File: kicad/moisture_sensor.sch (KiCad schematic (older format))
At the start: 17 parts, among them IC3 TLC555CDR, IC4 ADC081C021CIMK_NOPB, J11 SOIL_I2C, J18 ALWAYS_ON, Q1 DTC113Z

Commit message: Libraries cleanup
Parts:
- IC3: footprint SamacSys:SOIC127P600X175-8N -> SamacSys_Parts:SOIC127P600X175-8N; symbol SamaSys:TLC555CDR -> SamacSys_Parts:TLC555CDR
- IC4: footprint SamacSys:SOT95P280X110-6N -> SamacSys_Parts:SOT95P280X110-6N; symbol SamaSys:ADC081C021CIMK_NOPB -> SamacSys_Parts:ADC081C021CIMK_NOPB
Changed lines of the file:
@@
 $Descr A4 11693 8268
 encoding utf-8
-Sheet 3 6
+Sheet 3 7
 Title ""
 Date ""
@@
 	7450 3950 7450 4350
 $Comp
-L SamaSys:TLC555CDR IC3
+L SamacSys_Parts:TLC555CDR IC3
 U 1 1 5F161298
 P 7550 3850
 F 0 "IC3" H 8150 3850 50  0000 C CNN
 F 1 "TLC555CDR" H 8150 3400 50  0000 C CNN
-F 2 "SamacSys:SOIC127P600X175-8N" H 8600 3950 50  0001 L CNN
+F 2 "SamacSys_Parts:SOIC127P600X175-8N" H 8600 3950 50  0001 L CNN
 F 3 "" H 8600 3850 50  0001 L CNN
 F 4 "TLC555CDR, Timer 2MHz, 2 ??? 15 V, 8-Pin SOIC-8" H 8600 3750 50  0001 L CNN "Description"
@@
 	7150 2750 7600 2750
 $Comp
-L SamaSys:ADC081C021CIMK_NOPB IC4
+L SamacSys_Parts:ADC081C021CIMK_NOPB IC4
 U 1 1 5EFC5A0F
 P 7600 2550
 F 0 "IC4" H 8150 2815 50  0000 C CNN
 F 1 "ADC081C021CIMK_NOPB" H 8150 2724 50  0000 C CNN
-F 2 "SamacSys:SOT95P280X110-6N" H 8550 2650 50  0001 L CNN
+F 2 "SamacSys_Parts:SOT95P280X110-6N" H 8550 2650 50  0001 L CNN
 F 3 "http://www.ti.com/lit/ds/symlink/adc081c021.pdf" H 8550 2550 50  0001 L CNN
 F 4 "I2C-Compatible, 8-Bit Analog-to-Digital Converter with Alert Pin" H 8550 2450 50  0001 L CNN "Description"

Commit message: Comitting yesterday's leftovers
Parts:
- renumbered C3 to C5, C7 to C6, C4 to C7, C5 to C8, D1 to D4, IC3 to IC1, IC4 to IC2, J11 to J7, J18 to J8, R5 to R14, R4 to R15
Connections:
- net VA renamed +3.3VA
- net VDD renamed +3V3
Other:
- moved on the sheet: C5, C6, C7, C8, Cref1, D4, FB1, FB2, IC1, IC2, J7, J8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

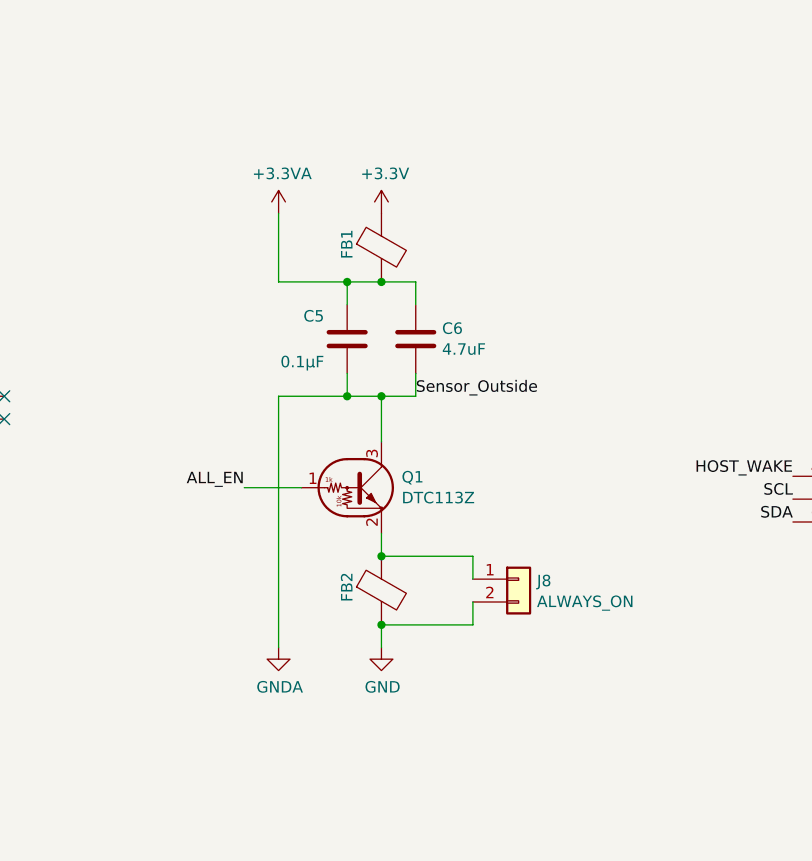
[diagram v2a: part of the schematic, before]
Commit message: Mapped footprints, PCB in progress
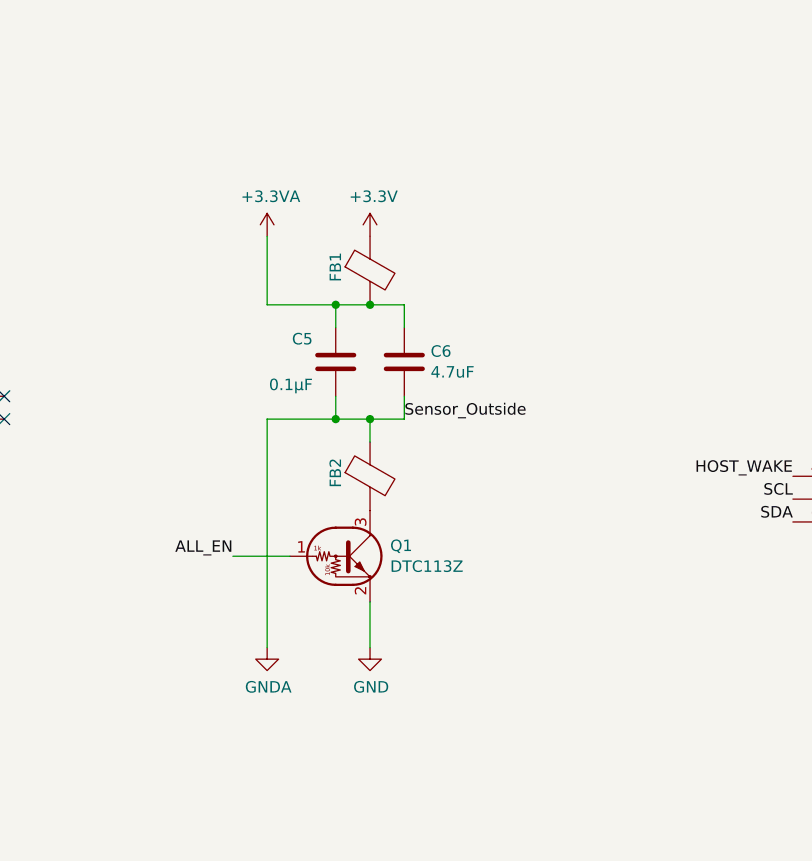
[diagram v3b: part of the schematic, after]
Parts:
- removed J8: ALWAYS_ON, Connector_PinHeader_2.54mm:PinHeader_1x02_P2.54mm_Vertical, symbol Connector_Generic:Conn_01x02
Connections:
- net GND: now also Q1.2 (E); no longer FB2.2
- net GNDA: now also FB2.1; no longer Q1.3 (C)
- new net: FB2.2, Q1.3 (C)
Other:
- moved on the sheet: C5, C6, FB1, FB2, Q1
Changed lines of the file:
@@
 L Device:C C5
 U 1 1 5F16FB60
-P 4050 3450
-F 0 "C5" H 4150 3350 50  0000 L CNN
-F 1 "0.1μF" H 4150 3550 50  0000 L CNN
-F 2 "Capacitor_SMD:C_1206_3216Metric" H 4088 3300 50  0001 C CNN
-F 3 "~" H 4050 3450 50  0001 C CNN
-	1    4050 3450
+P 4000 3550
+F 0 "C5" H 4100 3450 50  0000 L CNN
+F 1 "0.1μF" H 4100 3650 50  0000 L CNN
+F 2 "Capacitor_SMD:C_1206_3216Metric" H 4038 3400 50  0001 C CNN
+F 3 "~" H 4000 3550 50  0001 C CNN
+	1    4000 3550
 	-1   0    0    1
 $EndComp
@@
 	8750 3600 9500 3600
 Wire Wire Line
-	4350 3600 4350 3700
-Wire Wire Line
-	4050 3700 4050 3600
-Wire Wire Line
-	4050 3200 4050 3300
+	4300 3700 4300 3800
+Wire Wire Line
+	4000 3800 4000 3700
+Wire Wire Line
+	4000 3300 4000 3400
 Text Label 8550 4050 3    50   ~ 0
 Sensor_Inside
-Text Label 4350 3700 0    50   ~ 0
+Text Label 4300 3800 0    50   ~ 0
 Sensor_Outside
 Text Notes 7400 7500 0    50   ~ 0
@@
 Moisture Sensor
 $Comp
-L Transistor_BJT:DTC113Z Q1
-U 1 1 5F30B926
-P 4100 4100
-F 0 "Q1" H 4288 4146 50  0000 L CNN
-F 1 "DTC113Z" H 4288 4055 50  0000 L CNN
-F 2 "Parts:DTC113ZEBTL" H 4100 4100 50  0001 L CNN
-F 3 "" H 4100 4100 50  0001 L CNN
-	1    4100 4100
-	1    0    0    -1
-$EndComp
-$Comp
 L Device:Ferrite_Bead FB1
 U 1 1 5F30F8CD
-P 4200 3050
-F 0 "FB1" V 4050 3000 50  0000 L CNN
-F 1 "BLM21AG601SZ1D" V 4350 2900 50  0001 L CNN
-F 2 "Parts:Ferrite_Bead_0805_BLM21" V 4130 3050 50  0001 C CNN
-F 3 "https://www.mouser.com/datasheet/2/281/QNFA9114-1485065.pdf" H 4200 3050 50  0001 C CNN
-	1    4200 3050
-	1    0    0    -1
-$EndComp
-Wire Wire Line
-	4350 3200 4200 3200
-Connection ~ 4200 3200
-Wire Wire Line
-	4200 3200 4050 3200
+P 4150 3150
+F 0 "FB1" V 4000 3100 50  0000 L CNN
+F 1 "BLM21AG601SZ1D" V 4300 3000 50  0001 L CNN
+F 2 "Parts:Ferrite_Bead_0805_BLM21" V 4080 3150 50  0001 C CNN
+F 3 "https://www.mouser.com/datasheet/2/281/QNFA9114-1485065.pdf" H 4150 3150 50  0001 C CNN
+	1    4150 3150
+	1    0    0    -1
+$EndComp
+Wire Wire Line
+	4300 3300 4150 3300
+Connection ~ 4150 3300
+Wire Wire Line
+	4150 3300 4000 3300
 $Comp
 L power:GND #PWR?
@@
 NoConn ~ 2550 3700
 NoConn ~ 2550 3800
-Text Label 3600 4100 2    50   ~ 0
+Text Label 3550 4400 2    50   ~ 0
 ALL_EN
 $Comp
@@
 $EndComp
 Wire Wire Line
-	4350 3300 4350 3200
+	4300 3400 4300 3300
 $Comp
 L Device:C C6
 U 1 1 5FCEA2F8
-P 4350 3450
-F 0 "C6" H 4465 3496 50  0000 L CNN
-F 1 "4.7uF" H 4465 3405 50  0000 L CNN
-F 2 "Capacitor_SMD:C_1206_3216Metric" H 4388 3300 50  0001 C CNN
-F 3 "~" H 4350 3450 50  0001 C CNN
-	1    4350 3450
-	1    0    0    -1
-$EndComp
-Wire Wire Line
-	3600 4100 3850 4100
+P 4300 3550
+F 0 "C6" H 4415 3596 50  0000 L CNN
+F 1 "4.7uF" H 4415 3505 50  0000 L CNN
+F 2 "Capacitor_SMD:C_1206_3216Metric" H 4338 3400 50  0001 C CNN
+F 3 "~" H 4300 3550 50  0001 C CNN
+	1    4300 3550
+	1    0    0    -1
+$EndComp
 $Comp
 L power:+3.3V #PWR035
@@
 L power:+3.3V #PWR031
 U 1 1 6115F35B
-P 4200 2900
-F 0 "#PWR031" H 4200 2750 50  0001 C CNN
-F 1 "+3.3V" H 4215 3073 50  0000 C CNN
-F 2 "" H 4200 2900 50  0001 C CNN
-F 3 "" H 4200 2900 50  0001 C CNN
-	1    4200 2900
-	1    0    0    -1
-$EndComp
-Wire Wire Line
-	4050 3700 4200 3700
-Wire Wire Line
-	4200 3700 4200 3900
-Connection ~ 4200 3700
-Wire Wire Line
-	4200 3700 4350 3700
+P 4150 3000
+F 0 "#PWR031" H 4150 2850 50  0001 C CNN
+F 1 "+3.3V" H 4165 3173 50  0000 C CNN
+F 2 "" H 4150 3000 50  0001 C CNN
+F 3 "" H 4150 3000 50  0001 C CNN
+	1    4150 3000
+	1    0    0    -1
+$EndComp
 $Comp
 L power:GNDA #PWR028
@@
 $EndComp
 Wire Wire Line
-	4050 3700 3750 3700
-Connection ~ 4050 3700
+	4000 3800 3700 3800
+Connection ~ 4000 3800
 Text Label 6000 4050 2    50   ~ 0
 HOST_WAKE
@@
 L power:+3.3VA #PWR030
 U 1 1 611E3CB4
-P 3750 2900
-F 0 "#PWR030" H 3750 2750 50  0001 C CNN
-F 1 "+3.3VA" H 3765 3073 50  0000 C CNN
-F 2 "" H 3750 2900 50  0001 C CNN
-F 3 "" H 3750 2900 50  0001 C CNN
-	1    3750 2900
-	1    0    0    -1
-$EndComp
-Wire Wire Line
-	3750 2900 3750 3200
-Connection ~ 4050 3200
+P 3700 3000
+F 0 "#PWR030" H 3700 2850 50  0001 C CNN
+F 1 "+3.3VA" H 3715 3173 50  0000 C CNN
+F 2 "" H 3700 3000 50  0001 C CNN
+F 3 "" H 3700 3000 50  0001 C CNN
+	1    3700 3000
+	1    0    0    -1
+$EndComp
+Wire Wire Line
+	3700 3000 3700 3300
+Connection ~ 4000 3300
 $Comp
 L power:+3.3VA #PWR033
@@
 L power:GNDA #PWR036
 U 1 1 61222E66
-P 3750 4800
-F 0 "#PWR036" H 3750 4550 50  0001 C CNN
-F 1 "GNDA" H 3755 4627 50  0000 C CNN
-F 2 "" H 3750 4800 50  0001 C CNN
-F 3 "" H 3750 4800 50  0001 C CNN
-	1    3750 4800
-	1    0    0    -1
-$EndComp
-Wire Wire Line
-	3750 3700 3750 4800
-Wire Wire Line
-	3750 3200 4050 3200
-Wire Wire Line
-	4200 4300 4200 4400
-Wire Wire Line
-	4600 4700 4200 4700
-Wire Wire Line
-	4600 4600 4600 4700
-Wire Wire Line
-	4600 4400 4600 4500
-Wire Wire Line
-	4200 4400 4600 4400
-$Comp
-L Connector_Generic:Conn_01x02 J8
-U 1 1 5F4FBEBB
-P 4800 4500
-F 0 "J8" H 4880 4492 50  0000 L CNN
-F 1 "ALWAYS_ON" H 4880 4401 50  0000 L CNN
-F 2 "Connector_PinHeader_2.54mm:PinHeader_1x02_P2.54mm_Vertical" H 4800 4500 50  0001 C CNN
-F 3 "~" H 4800 4500 50  0001 C CNN
-	1    4800 4500
+P 3700 4800
+F 0 "#PWR036" H 3700 4550 50  0001 C CNN
+F 1 "GNDA" H 3705 4627 50  0000 C CNN
+F 2 "" H 3700 4800 50  0001 C CNN
+F 3 "" H 3700 4800 50  0001 C CNN
+	1    3700 4800
+	1    0    0    -1
+$EndComp
+Wire Wire Line
+	3700 3300 4000 3300
+Wire Wire Line
+	4000 3800 4150 3800
+Wire Wire Line
+	4150 4600 4150 4800
+$Comp
+L power:GND #PWR037
+U 1 1 5F30EBF5
+P 4150 4800
+F 0 "#PWR037" H 4150 4550 50  0001 C CNN
+F 1 "GND" H 4155 4627 50  0000 C CNN
+F 2 "" H 4150 4800 50  0001 C CNN
+F 3 "" H 4150 4800 50  0001 C CNN
+	1    4150 4800
 	1    0    0    -1
 $EndComp
@@
 L Device:Ferrite_Bead FB2
 U 1 1 5F343F65
-P 4200 4550
-F 0 "FB2" V 4050 4500 50  0000 L CNN
-F 1 "BLM21AG601SZ1D" V 4350 4300 50  0001 L CNN
-F 2 "Parts:Ferrite_Bead_0805_BLM21" V 4130 4550 50  0001 C CNN
-F 3 "https://www.mouser.com/datasheet/2/281/QNFA9114-1485065.pdf" H 4200 4550 50  0001 C CNN
-	1    4200 4550
-	1    0    0    -1
-$EndComp
-$Comp
-L power:GND #PWR037
-U 1 1 5F30EBF5
-P 4200 4800
-F 0 "#PWR037" H 4200 4550 50  0001 C CNN
-F 1 "GND" H 4205 4627 50  0000 C CNN
-F 2 "" H 4200 4800 50  0001 C CNN
-F 3 "" H 4200 4800 50  0001 C CNN
-	1    4200 4800
-	1    0    0    -1
-$EndComp
-Connection ~ 4200 4400
-Wire Wire Line
-	4200 4700 4200 4800
-Connection ~ 4200 4700
+P 4150 4050
+F 0 "FB2" V 4000 4000 50  0000 L CNN
+F 1 "BLM21AG601SZ1D" V 4300 3800 50  0001 L CNN
+F 2 "Parts:Ferrite_Bead_0805_BLM21" V 4080 4050 50  0001 C CNN
+F 3 "https://www.mouser.com/datasheet/2/281/QNFA9114-1485065.pdf" H 4150 4050 50  0001 C CNN
+	1    4150 4050
+	1    0    0    -1
+$EndComp
+Wire Wire Line
+	3550 4400 3800 4400
+$Comp
+L Transistor_BJT:DTC113Z Q1
+U 1 1 5F30B926
+P 4050 4400
+F 0 "Q1" H 4238 4446 50  0000 L CNN
+F 1 "DTC113Z" H 4238 4355 50  0000 L CNN
+F 2 "Parts:DTC113ZEBTL" H 4050 4400 50  0001 L CNN
+F 3 "" H 4050 4400 50  0001 L CNN
+	1    4050 4400
+	1    0    0    -1
+$EndComp
+Wire Wire Line
+	3700 3800 3700 4800
+Wire Wire Line
+	4150 3800 4150 3900
+Connection ~ 4150 3800
+Wire Wire Line
+	4150 3800 4300 3800
 $EndSCHEMATC
